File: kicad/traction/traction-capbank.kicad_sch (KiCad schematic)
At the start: 26 parts

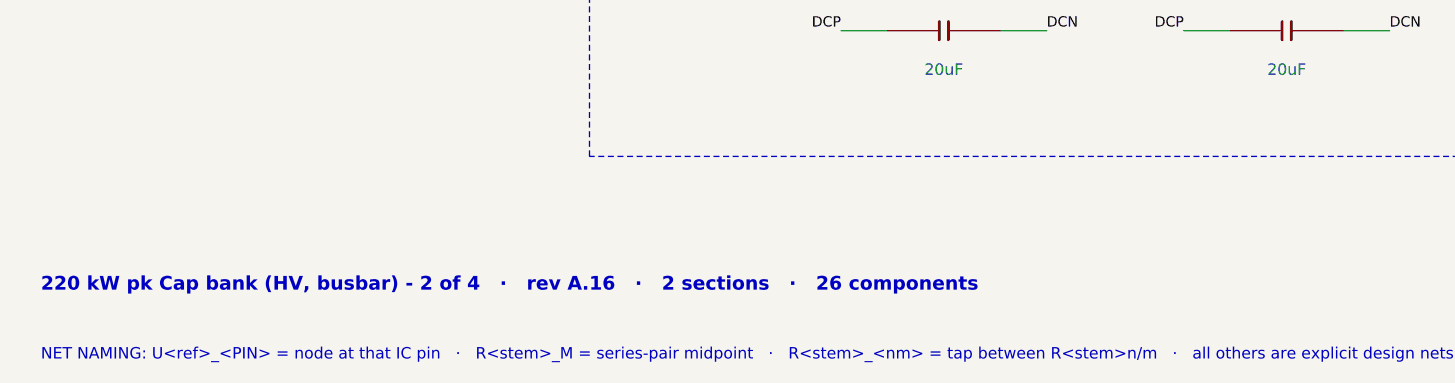
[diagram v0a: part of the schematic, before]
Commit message: Rev A.17: round 18 — three rechecks of 4425af9 (F190-F198): diversion diodes on the amplifier node (loop passes RSX), diode cell cathode = pin 1 on all 35 diodes, exciter TVS/PTC rows at worst corners + ECU-asleep sustained short (WARN rows, layout rule, QP-RX-04 2b gate), anti-surge RSX, NCV4276C reverse current = QP-RX-05 gate + VR-33, IR-16/IR-42, firmware FW-34..36 (sample freshness, cadence-locked resolver frames, latency sign) + three self-found instances
Co-Authored-By: Claude Fable 5.1 <noreply@anthropic.com>
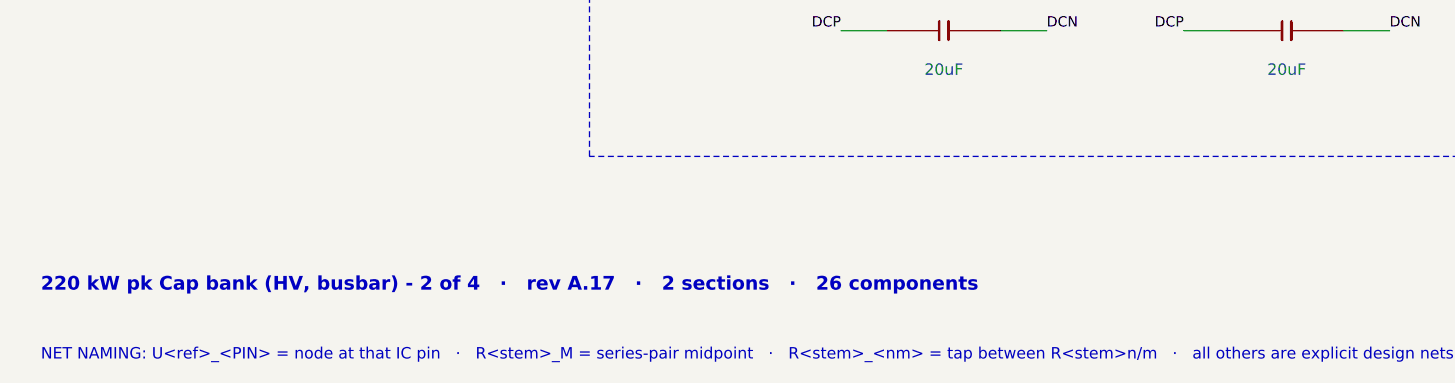
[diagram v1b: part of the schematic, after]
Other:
- note added: "220 kW pk Cap bank (HV, busbar) - 2 of 4 · rev A.17 · 2 sections · 26 components"
- note removed: "220 kW pk Cap bank (HV, busbar) - 2 of 4 · rev A.16 · 2 sections · 26 components"
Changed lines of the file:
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@@
 		(title "Traction Inverter — Cap bank (busbar assembly, 320 uF)")
 		(date "2026-09-23")
-		(rev "A.16")
+		(rev "A.17")
 		(company "Traction Inverter 220 kW pk - Cap bank (HV, busbar), sheet 2 of 4")
 		(comment 1 "Inverter = Power board + Cap bank busbar + bolt-on Discharge board (all HV) + Control card (LV); safe state holds with any link lost")
@@
 	(rectangle (start 12.7 12.7) (end 66.04 95.25) (stroke (width 0) (type dash)) (fill (type none)))
 	(rectangle (start 76.2 12.7) (end 193.04 114.3) (stroke (width 0) (type dash)) (fill (type none)))
-	(text "220 kW pk Cap bank (HV, busbar) - 2 of 4   ·   rev A.16   ·   2 sections   ·   26 components" (exclude_from_sim no) (at 15.24 129.54 0) (effects (font (size 1.524 1.524) (bold yes)) (justify left bottom)))
+	(text "220 kW pk Cap bank (HV, busbar) - 2 of 4   ·   rev A.17   ·   2 sections   ·   26 components" (exclude_from_sim no) (at 15.24 129.54 0) (effects (font (size 1.524 1.524) (bold yes)) (justify left bottom)))
 	(text "NET NAMING: U<ref>_<PIN> = node at that IC pin   ·   R<stem>_M = series-pair midpoint   ·   R<stem>_<nm> = tap between R<stem>n/m   ·   all others are explicit design nets   ·   same name on another sheet = same net, joined only at the named connector/stud/tab" (exclude_from_sim no) (at 15.24 137.16 0) (effects (font (size 1.27 1.27)) (justify left bottom)))
 	(text "CAP-BANK / BUS-STUDS" (exclude_from_sim no) (at 14.224 16.764 0) (effects (font (size 2.0066 2.0066) (bold yes)) (justify left bottom)))

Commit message: Rev A.18: round 19 — three rechecks of e315bf1 (F199-F204): PTC-current row at every permitted voltage (IR-16 0.08/0.14/0.37/0.26 Ω), ≥8 A TVS energy an explicit assumption + QP-RX-04 release criterion, window criterion fixed, exciter TVS → SMDJ7.0A-HRA (coupled island holds the 7.0 V class at a parked 12 V battery / the Marine rail), shared exciter-fault model run for the Marine port (QP-MA-11, kit-loom rule), FW-35 rewritten on an SWG-anchored time origin with clock-derived resync and bounded restart
Co-Authored-By: Claude Fable 5.1 <noreply@anthropic.com>
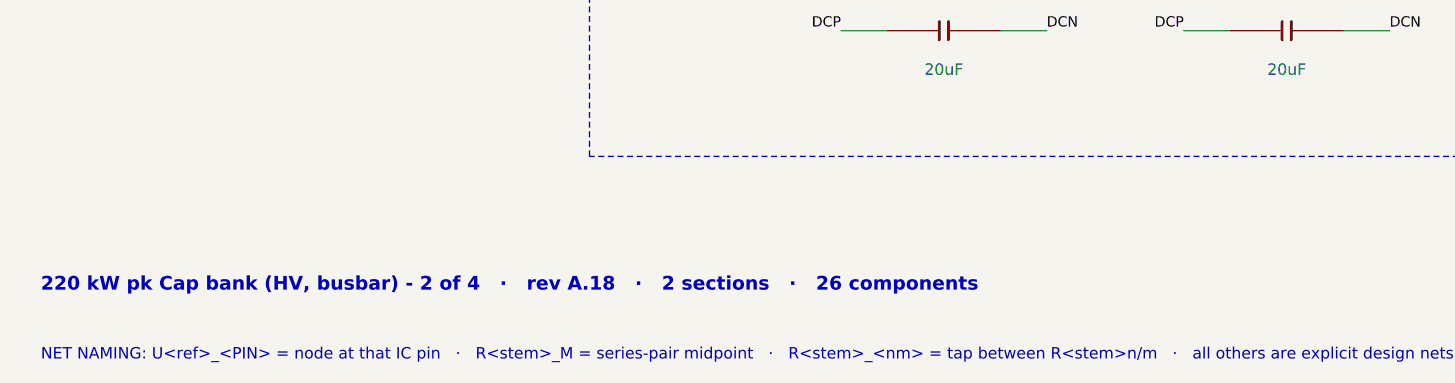
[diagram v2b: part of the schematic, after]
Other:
- note added: "220 kW pk Cap bank (HV, busbar) - 2 of 4 · rev A.18 · 2 sections · 26 components"
- note removed: "220 kW pk Cap bank (HV, busbar) - 2 of 4 · rev A.17 · 2 sections · 26 components"
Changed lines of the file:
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@@
 		(title "Traction Inverter — Cap bank (busbar assembly, 320 uF)")
 		(date "2026-09-23")
-		(rev "A.17")
+		(rev "A.18")
 		(company "Traction Inverter 220 kW pk - Cap bank (HV, busbar), sheet 2 of 4")
 		(comment 1 "Inverter = Power board + Cap bank busbar + bolt-on Discharge board (all HV) + Control card (LV); safe state holds with any link lost")
@@
 	(rectangle (start 12.7 12.7) (end 66.04 95.25) (stroke (width 0) (type dash)) (fill (type none)))
 	(rectangle (start 76.2 12.7) (end 193.04 114.3) (stroke (width 0) (type dash)) (fill (type none)))
-	(text "220 kW pk Cap bank (HV, busbar) - 2 of 4   ·   rev A.17   ·   2 sections   ·   26 components" (exclude_from_sim no) (at 15.24 129.54 0) (effects (font (size 1.524 1.524) (bold yes)) (justify left bottom)))
+	(text "220 kW pk Cap bank (HV, busbar) - 2 of 4   ·   rev A.18   ·   2 sections   ·   26 components" (exclude_from_sim no) (at 15.24 129.54 0) (effects (font (size 1.524 1.524) (bold yes)) (justify left bottom)))
 	(text "NET NAMING: U<ref>_<PIN> = node at that IC pin   ·   R<stem>_M = series-pair midpoint   ·   R<stem>_<nm> = tap between R<stem>n/m   ·   all others are explicit design nets   ·   same name on another sheet = same net, joined only at the named connector/stud/tab" (exclude_from_sim no) (at 15.24 137.16 0) (effects (font (size 1.27 1.27)) (justify left bottom)))
 	(text "CAP-BANK / BUS-STUDS" (exclude_from_sim no) (at 14.224 16.764 0) (effects (font (size 2.0066 2.0066) (bold yes)) (justify left bottom)))

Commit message: Rev A.19: round 20 — three rechecks of 00f6252 (F205-F207): TVS alternate to the 7.0 V class + lock, 4XX discharge alternate 470→220 Ω + lock, T-05/T-06 firmware ID, 8.5 V-era figures re-derived at the IR-16 allocations
Co-Authored-By: Claude Fable 5.1 <noreply@anthropic.com>
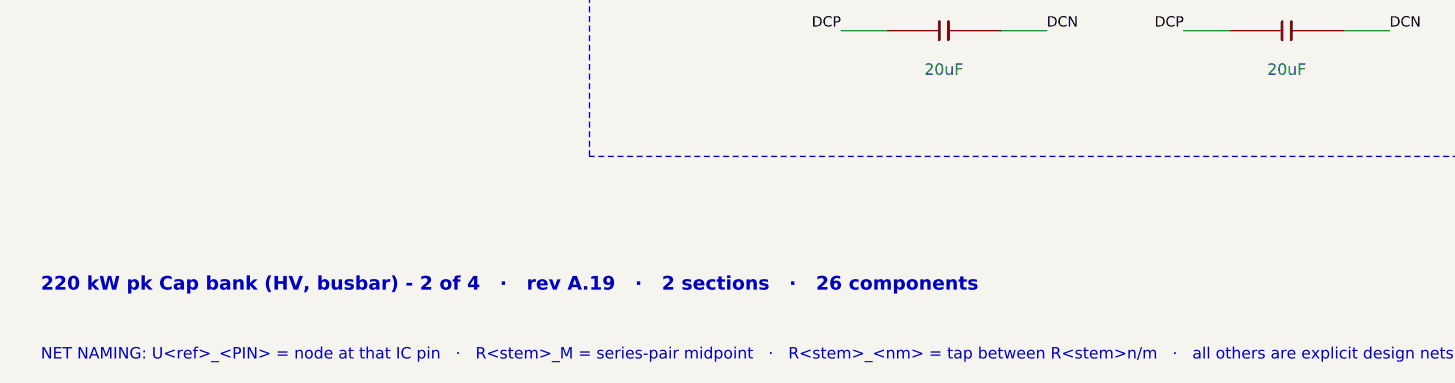
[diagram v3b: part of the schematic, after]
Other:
- note added: "220 kW pk Cap bank (HV, busbar) - 2 of 4 · rev A.19 · 2 sections · 26 components"
- note removed: "220 kW pk Cap bank (HV, busbar) - 2 of 4 · rev A.18 · 2 sections · 26 components"
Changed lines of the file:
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@@
 		(title "Traction Inverter — Cap bank (busbar assembly, 320 uF)")
 		(date "2026-09-23")
-		(rev "A.18")
+		(rev "A.19")
 		(company "Traction Inverter 220 kW pk - Cap bank (HV, busbar), sheet 2 of 4")
 		(comment 1 "Inverter = Power board + Cap bank busbar + bolt-on Discharge board (all HV) + Control card (LV); safe state holds with any link lost")
@@
 	(rectangle (start 12.7 12.7) (end 66.04 95.25) (stroke (width 0) (type dash)) (fill (type none)))
 	(rectangle (start 76.2 12.7) (end 193.04 114.3) (stroke (width 0) (type dash)) (fill (type none)))
-	(text "220 kW pk Cap bank (HV, busbar) - 2 of 4   ·   rev A.18   ·   2 sections   ·   26 components" (exclude_from_sim no) (at 15.24 129.54 0) (effects (font (size 1.524 1.524) (bold yes)) (justify left bottom)))
+	(text "220 kW pk Cap bank (HV, busbar) - 2 of 4   ·   rev A.19   ·   2 sections   ·   26 components" (exclude_from_sim no) (at 15.24 129.54 0) (effects (font (size 1.524 1.524) (bold yes)) (justify left bottom)))
 	(text "NET NAMING: U<ref>_<PIN> = node at that IC pin   ·   R<stem>_M = series-pair midpoint   ·   R<stem>_<nm> = tap between R<stem>n/m   ·   all others are explicit design nets   ·   same name on another sheet = same net, joined only at the named connector/stud/tab" (exclude_from_sim no) (at 15.24 137.16 0) (effects (font (size 1.27 1.27)) (justify left bottom)))
 	(text "CAP-BANK / BUS-STUDS" (exclude_from_sim no) (at 14.224 16.764 0) (effects (font (size 2.0066 2.0066) (bold yes)) (justify left bottom)))

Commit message: Rev A.20: round 21 — three rechecks of 551c405 (F208): stale 0.29 Ω in gate ㉘ and the QP-RX-04 fixture instruction → 0.37 Ω, last 8.5 V-era figures aligned, Marine sweep cross-references at the current values
Co-Authored-By: Claude Fable 5.1 <noreply@anthropic.com>
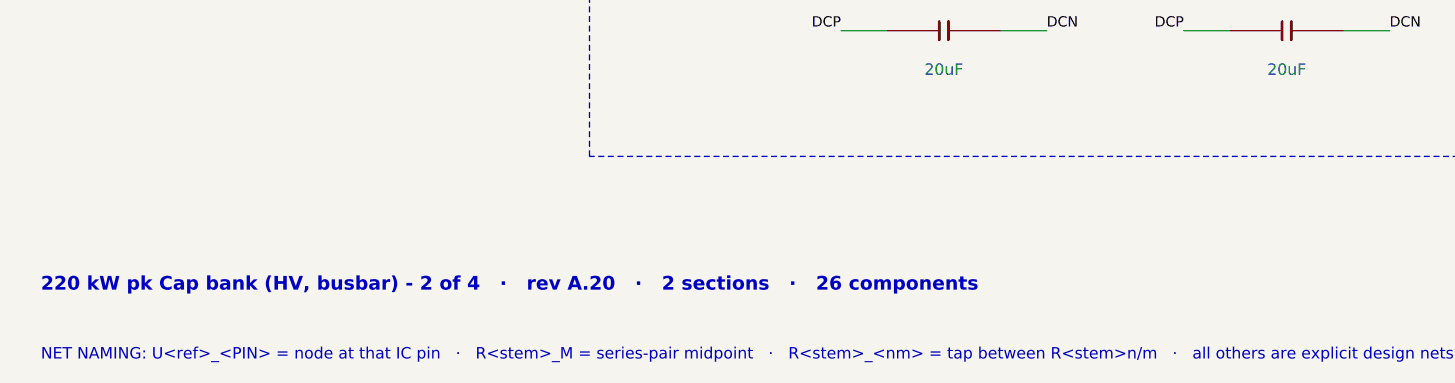
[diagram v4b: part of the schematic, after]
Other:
- note added: "220 kW pk Cap bank (HV, busbar) - 2 of 4 · rev A.20 · 2 sections · 26 components"
- note removed: "220 kW pk Cap bank (HV, busbar) - 2 of 4 · rev A.19 · 2 sections · 26 components"
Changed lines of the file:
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@@
 		(title "Traction Inverter — Cap bank (busbar assembly, 320 uF)")
 		(date "2026-09-23")
-		(rev "A.19")
+		(rev "A.20")
 		(company "Traction Inverter 220 kW pk - Cap bank (HV, busbar), sheet 2 of 4")
 		(comment 1 "Inverter = Power board + Cap bank busbar + bolt-on Discharge board (all HV) + Control card (LV); safe state holds with any link lost")
@@
 	(rectangle (start 12.7 12.7) (end 66.04 95.25) (stroke (width 0) (type dash)) (fill (type none)))
 	(rectangle (start 76.2 12.7) (end 193.04 114.3) (stroke (width 0) (type dash)) (fill (type none)))
-	(text "220 kW pk Cap bank (HV, busbar) - 2 of 4   ·   rev A.19   ·   2 sections   ·   26 components" (exclude_from_sim no) (at 15.24 129.54 0) (effects (font (size 1.524 1.524) (bold yes)) (justify left bottom)))
+	(text "220 kW pk Cap bank (HV, busbar) - 2 of 4   ·   rev A.20   ·   2 sections   ·   26 components" (exclude_from_sim no) (at 15.24 129.54 0) (effects (font (size 1.524 1.524) (bold yes)) (justify left bottom)))
 	(text "NET NAMING: U<ref>_<PIN> = node at that IC pin   ·   R<stem>_M = series-pair midpoint   ·   R<stem>_<nm> = tap between R<stem>n/m   ·   all others are explicit design nets   ·   same name on another sheet = same net, joined only at the named connector/stud/tab" (exclude_from_sim no) (at 15.24 137.16 0) (effects (font (size 1.27 1.27)) (justify left bottom)))
 	(text "CAP-BANK / BUS-STUDS" (exclude_from_sim no) (at 14.224 16.764 0) (effects (font (size 2.0066 2.0066) (bold yes)) (justify left bottom)))

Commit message: Rev A.21: round 22 — three rechecks of 0ff44d9 (F209) + the layout handoff (F210–F213): every KiCad symbol bound to a footprint in a shipped traction.pretty (45 verbatim KiCad-10 patterns + 18 datasheet-drawn), fp-lib-table and per-board projects in all sets, pad-per-pin KiCad proof; NCV4276C 5-lead lands, ALM2402/TPS55340 thermal-pad pins, 2-pad crystal; QP §0.2 baseline and stale IDs; docs/layout-handoff.md
Co-Authored-By: Claude Fable 5.1 <noreply@anthropic.com>
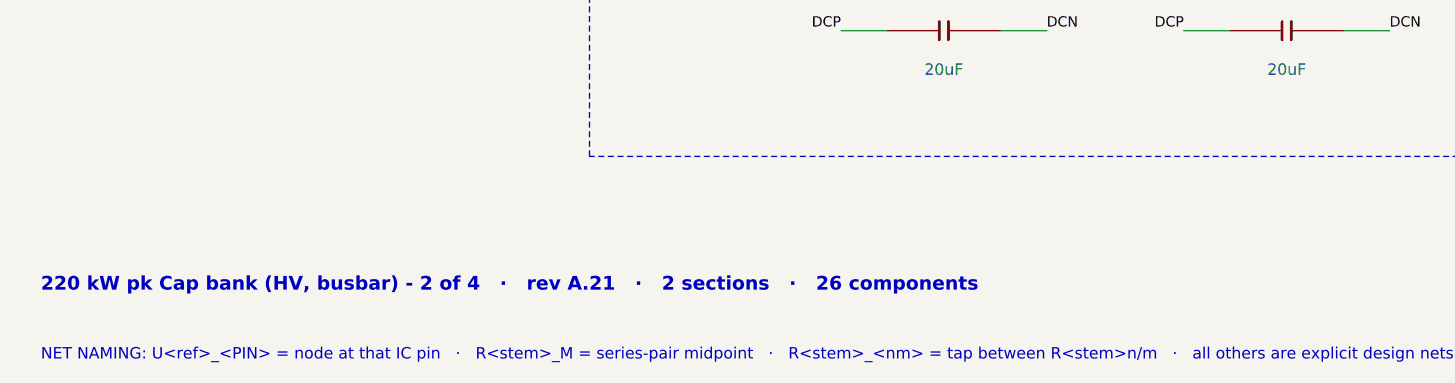
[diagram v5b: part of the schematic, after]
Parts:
- CDC1, CDC10, CDC11, CDC12, CDC13, CDC14, CDC15, CDC16, CDC2, CDC3, CDC4, CDC5, CDC6, CDC7, CDC8, CDC9: footprint FilmCan37.5 -> traction:Faratronic_C3D1_P37.5
- JCBDN, JCBDP: footprint StudM6 -> traction:MountingHole_6.4mm_M6_Pad
- JCBEN, JCBEP: footprint StudM8 -> traction:MountingHole_8.4mm_M8_Pad
- JCBUN, JCBUP, JCBVN, JCBVP, JCBWN, JCBWP: footprint TabM6 -> traction:MountingHole_6.4mm_M6_Pad
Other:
- note added: "220 kW pk Cap bank (HV, busbar) - 2 of 4 · rev A.21 · 2 sections · 26 components"
- note removed: "220 kW pk Cap bank (HV, busbar) - 2 of 4 · rev A.20 · 2 sections · 26 components"

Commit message: Rev A.22: round 23 — rechecks of 452de85 (F214–F220), the VESC program (FW-38…FW-46, Traction Tool in Qt) and the "why not done" extension (F221–F239)
Hardware: the R2R reference isolated at ball A9 (RR2R 10 Ω + 1 µF + 100 nF, S32K39 DS note 8), the SWD header on its
surface-mount Samtec land with a mounting-technology lock in the library generator, the footprint library declared
KiCad 10.0.6+ and no longer mirrored into the KiCad 5 sets; the BOM intro follows the SKU; a VREFH window row and VR-34/35.

Firmware (TI_FW_ID 0x0A0F0015, CAL layout 4, 190 fields / 91 CAL rows, 80 DTCs): FW-37 joint torque solve with a
postcondition; the VESC gap closure — FW-38 signed field update (Ed25519, anti-rollback, ISO-TP), FW-39 interlocked motor
self-commissioning, FW-40 UDS diagnostics (0x19/0x22/0x2A/0x14 over ISO 15765-2), FW-41 fault-triggered waveform capture,
FW-42 overspeed, FW-43 run-time statistics, FW-44 key-on offset adoption, FW-45 saturation-dependent inductance tables
with gain scheduling, FW-46 cogging feed-forward; twelve defects found by the closed-loop simulator bridge (F221–F232),
the 64-bit divide out of every ISR path with a link-time guard, the UDS escape single frame accepted by every service,
the root of trust reported (DID 0xFD23), the boot record, motor data and active maps as DIDs; 421 tests / 4937 checks /
0 failed on the host (-O1, -O2, ASan/UBSan, -ffp-contract=off) and on the Cortex-M7 under QEMU with the target compiler
(make qemu-test, T-59); make target-check 63 markers, make target-size with the divide guard.

Traction Tool (tool/): Qt 6 / C++17 Widgets + Qwt, offline; pages Dashboard, Live plots, Controls, Commissioning,
Parameters, Faults & alerts, Analysis, Terminal, Firmware; transports simulator bridge (tool/bridge, the real firmware
against a plant), log replay, CAN (QCanBus with ISO-TP both ways, proved against the firmware over the virtualcan bus);
the signed update end to end over both transports; the commissioning routines, the map sw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
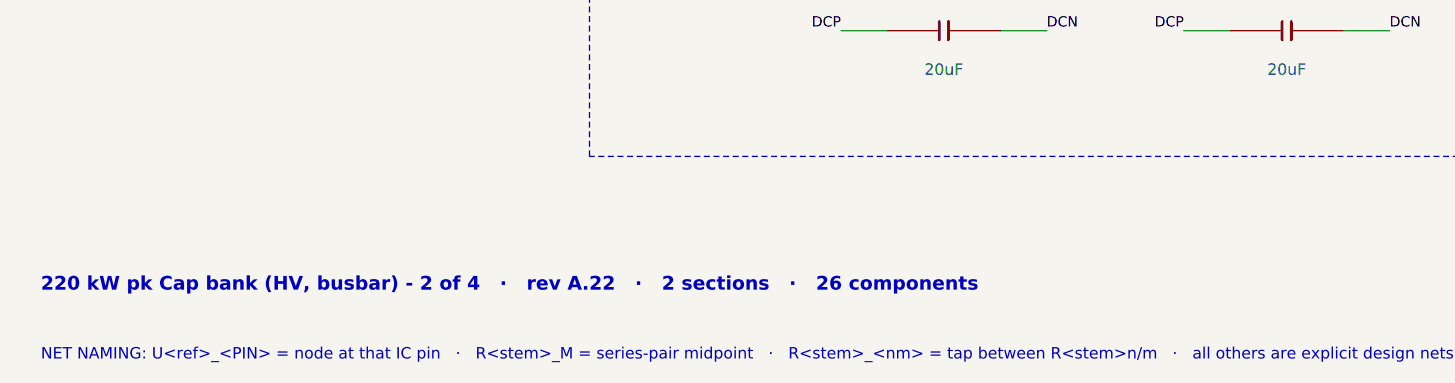
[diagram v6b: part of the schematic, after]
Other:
- note added: "220 kW pk Cap bank (HV, busbar) - 2 of 4 · rev A.22 · 2 sections · 26 components"
- note removed: "220 kW pk Cap bank (HV, busbar) - 2 of 4 · rev A.21 · 2 sections · 26 components"
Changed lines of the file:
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@@
 		(title "Traction Inverter — Cap bank (busbar assembly, 320 uF)")
 		(date "2026-09-23")
-		(rev "A.21")
+		(rev "A.22")
 		(company "Traction Inverter 220 kW pk - Cap bank (HV, busbar), sheet 2 of 4")
 		(comment 1 "Inverter = Power board + Cap bank busbar + bolt-on Discharge board (all HV) + Control card (LV); safe state holds with any link lost")
@@
 	(rectangle (start 12.7 12.7) (end 66.04 95.25) (stroke (width 0) (type dash)) (fill (type none)))
 	(rectangle (start 76.2 12.7) (end 193.04 114.3) (stroke (width 0) (type dash)) (fill (type none)))
-	(text "220 kW pk Cap bank (HV, busbar) - 2 of 4   ·   rev A.21   ·   2 sections   ·   26 components" (exclude_from_sim no) (at 15.24 129.54 0) (effects (font (size 1.524 1.524) (bold yes)) (justify left bottom)))
+	(text "220 kW pk Cap bank (HV, busbar) - 2 of 4   ·   rev A.22   ·   2 sections   ·   26 components" (exclude_from_sim no) (at 15.24 129.54 0) (effects (font (size 1.524 1.524) (bold yes)) (justify left bottom)))
 	(text "NET NAMING: U<ref>_<PIN> = node at that IC pin   ·   R<stem>_M = series-pair midpoint   ·   R<stem>_<nm> = tap between R<stem>n/m   ·   all others are explicit design nets   ·   same name on another sheet = same net, joined only at the named connector/stud/tab" (exclude_from_sim no) (at 15.24 137.16 0) (effects (font (size 1.27 1.27)) (justify left bottom)))
 	(text "CAP-BANK / BUS-STUDS" (exclude_from_sim no) (at 14.224 16.764 0) (effects (font (size 2.0066 2.0066) (bold yes)) (justify left bottom)))
